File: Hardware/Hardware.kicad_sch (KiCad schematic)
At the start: 46 parts, among them J1 ILI9341, J2 RJ45_LED_Shielded, J3 USB_A, J5 Conn_01x06_Pin, SW1 SW_SPST, SW14 SW_Push, SW2 SW_Push, SW3 SW_Push, SW4 SW_Push, SW5 SW_Push, SW6 SW_Push, SW7 SW_Push, U1 TMR-0511, U2 ATA6561, U3 Teensy4.1_DEV-16771, U4 ESP32-WROOM-32UE, U5 ASSR-1218, U6 ASSR-1218

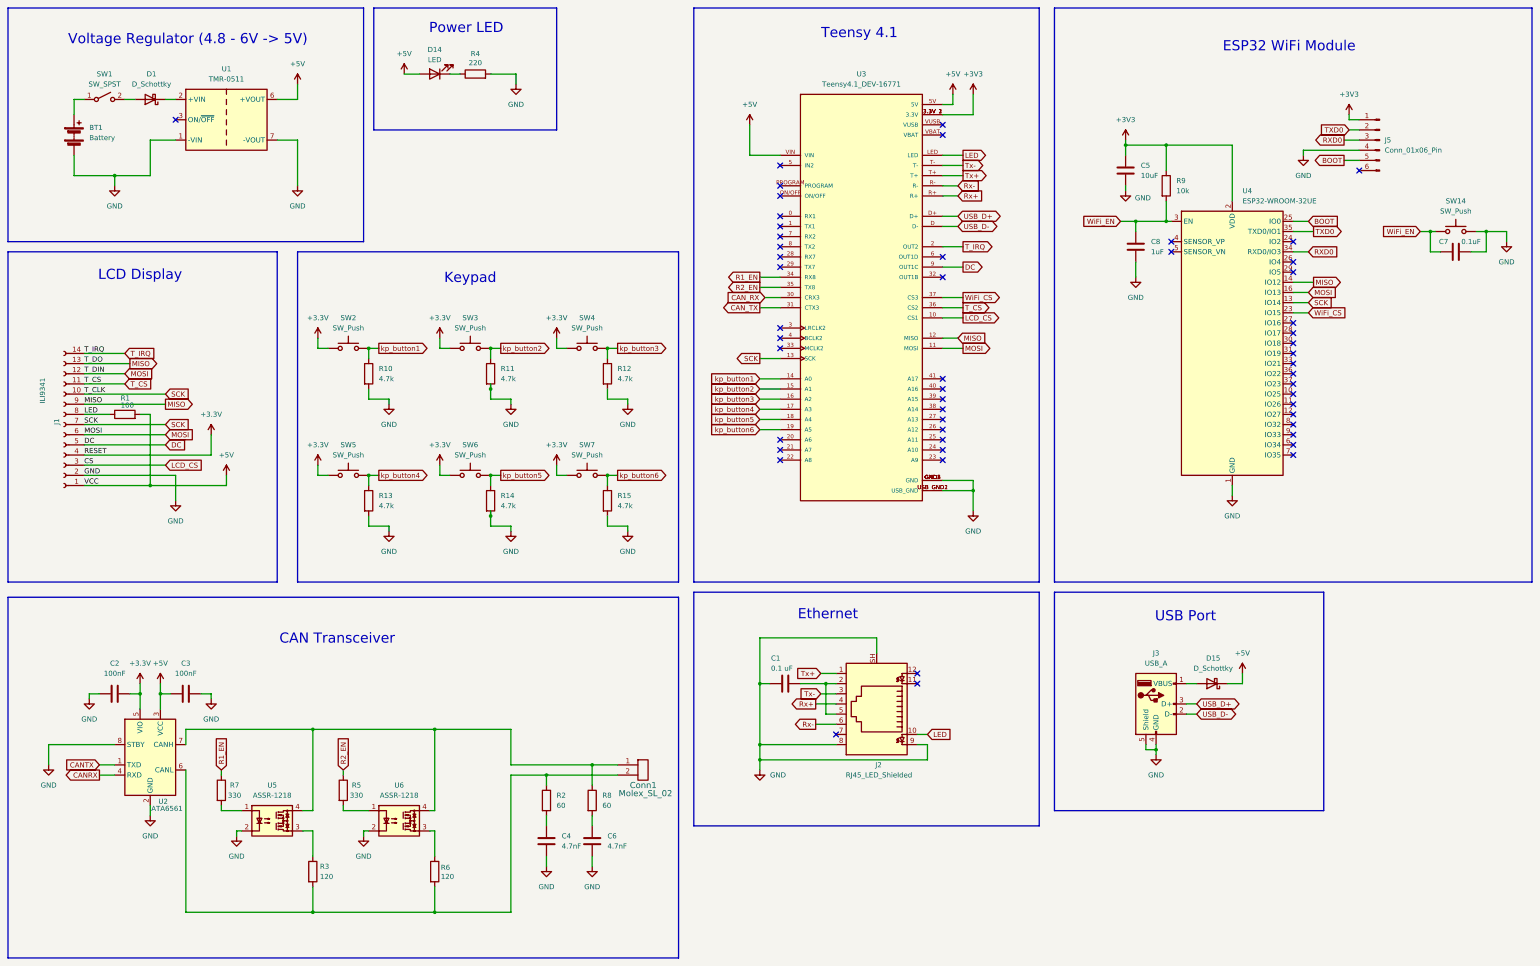
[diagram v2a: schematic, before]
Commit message: added mounting holes and fixed stuff
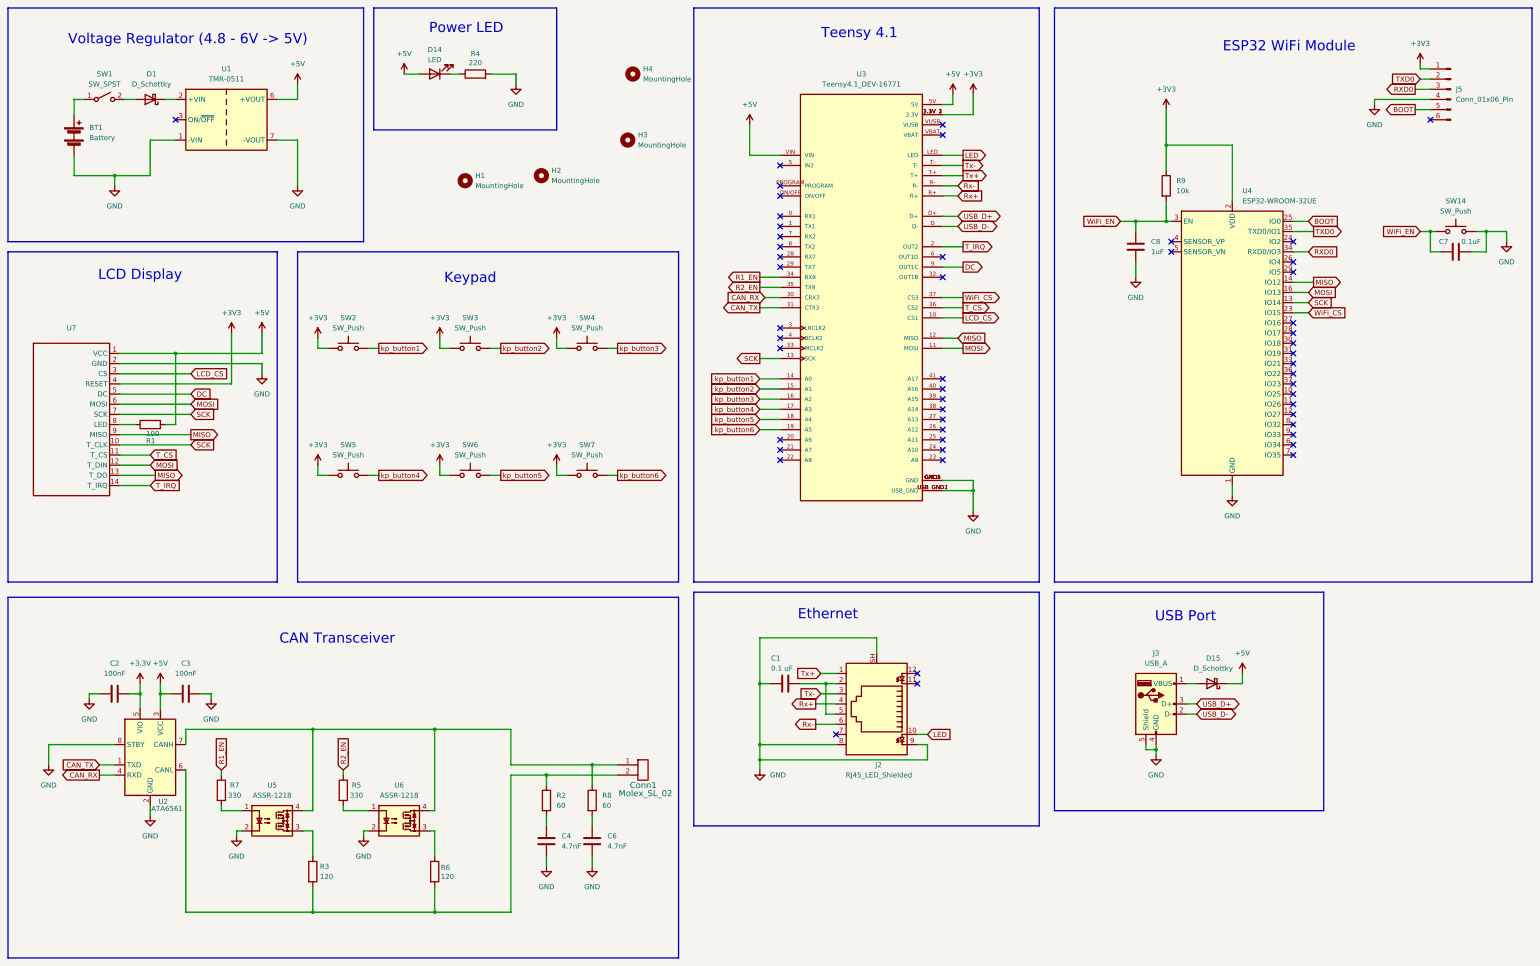
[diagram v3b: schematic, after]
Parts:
- removed C5: 10uF, Capacitor_SMD:C_0603_1608Metric_Pad1.08x0.95mm_HandSolder, symbol Device:C
- removed J1: ILI9341, Connector_PinSocket_2.54mm:PinSocket_1x14_P2.54mm_Vertical, symbol Connector:Conn_01x14_Socket
- removed R10, R11, R12, R13, R14, R15: 4.7k, Resistor_SMD:R_0603_1608Metric_Pad0.98x0.95mm_HandSolder, symbol Device:R
- added H1, H2, H3, H4: MountingHole, MRDT_Drill_Holes:4_40_Hole, symbol Mechanical:MountingHole
- added U7: ~, sw_spst:DISPLAY_ILI9341_TOUCH_32, symbol sw_spst:DISPLAY_ILI9341_TOUCH_32
- BT1: footprint Connector_Wire:SolderWire-0.15sqmm_1x02_P4mm_D0.5mm_OD1.5mm_Relief -> MRDT_Connectors:MOLEX_SL_02_Horizontal
- Conn1: footprint MRDT_Connectors:MOLEX_SL_02_Vertical -> MRDT_Connectors:MOLEX_SL_02_Horizontal
- SW1: footprint sw_spst:SOIC450P1000X730-4N -> Button_Switch_THT:SW_Slide_SPDT_Angled_CK_OS102011MA1Q
- U3: footprint MRDT_Shields:Teensy_4_1_Ethernet -> MRDT_Shields:Teensy_4_1
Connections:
- net CANRX is gone; now on net CAN_RX: U2.4 (RXD)
- net CANTX is gone; now on net CAN_TX: U2.1 (TXD)
- net +3.3V: no longer SW2.1, SW3.1, SW4.1, SW5.1, SW6.1, SW7.1
- net +3V3: now also SW2.1, SW3.1, SW4.1, SW5.1, SW6.1, SW7.1, U7.4 (RESET)
- net +5V: now also U7.1 (VCC)
- net DC: now also U7.5 (DC)
- net GND: now also U7.2 (GND)
- net LCD_CS: now also U7.3 (CS)
- net LED: no longer R1.1
- net MISO: now also U7.13 (T_DO), U7.9 (MISO)
- net MOSI: now also U7.12 (T_DIN), U7.6 (MOSI)
- net SCK: now also U7.10 (T_CLK), U7.7 (SCK)
- net T_CS: now also U7.11 (T_CS)
- net T_IRQ: now also U7.14 (T_IRQ)
- new net: R1.1, U7.8 (LED)
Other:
- moved on the sheet: J5, R1

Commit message: finished up the layout and cleaned up libraries
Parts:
- removed C7: 0.1uF, Capacitor_SMD:C_0603_1608Metric_Pad1.08x0.95mm_HandSolder, symbol Device:C
- removed D1, D15: D_Schottky, MRDT_Passives:SOT-23_Diode, symbol Device:D_Schottky
- added D1, D2: D_Schottky_ZLLS500, Tester:D_Schottky_ZLLS500, symbol Tester:D_Schottky_ZLLS500
- added H5, H6: MountingHole, MRDT_Drill_Holes:4_40_Hole, symbol Mechanical:MountingHole
- SW2, SW3, SW4, SW5, SW6, SW7: footprint Button_Switch_SMD:SW_SPST_TL3305A -> Tester:SW_SPST_TL3301
- U7: footprint sw_spst:DISPLAY_ILI9341_TOUCH_32 -> Tester:DISPLAY_ILI9341_TOUCH_32
- renumbered C6 to C5, C8 to C6, D14 to D3, SW14 to SW8
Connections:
- net +3V3: no longer SW2.1, SW3.1, SW4.1, SW5.1, SW6.1, SW7.1
- net +5V: now also D2.1 (K)
- net GND: now also SW2.1, SW3.1, SW4.1, SW5.1, SW6.1, SW7.1
- net WiFi_EN: now also U3.33 (MCLK2)
- net at SW1.2 (B): now also D1.3 (A)
- net at J3.1 (VBUS): now also D2.3 (A)
- net at U1.2 (+VIN): now also D1.1 (K)
- net kp_button1 renamed KP_ACCEPT
- net kp_button2 renamed KP_BACK
- net kp_button3 renamed KP_RIGHT
- net kp_button4 renamed KP_DOWN
- net KP_DOWN: now also SW6.2; no longer SW5.2
- net kp_button5 renamed KP_UP
- net KP_UP: now also SW5.2; no longer SW6.2
- net kp_button6 renamed KP_LEFT
- no-connect marks 52 -> 51

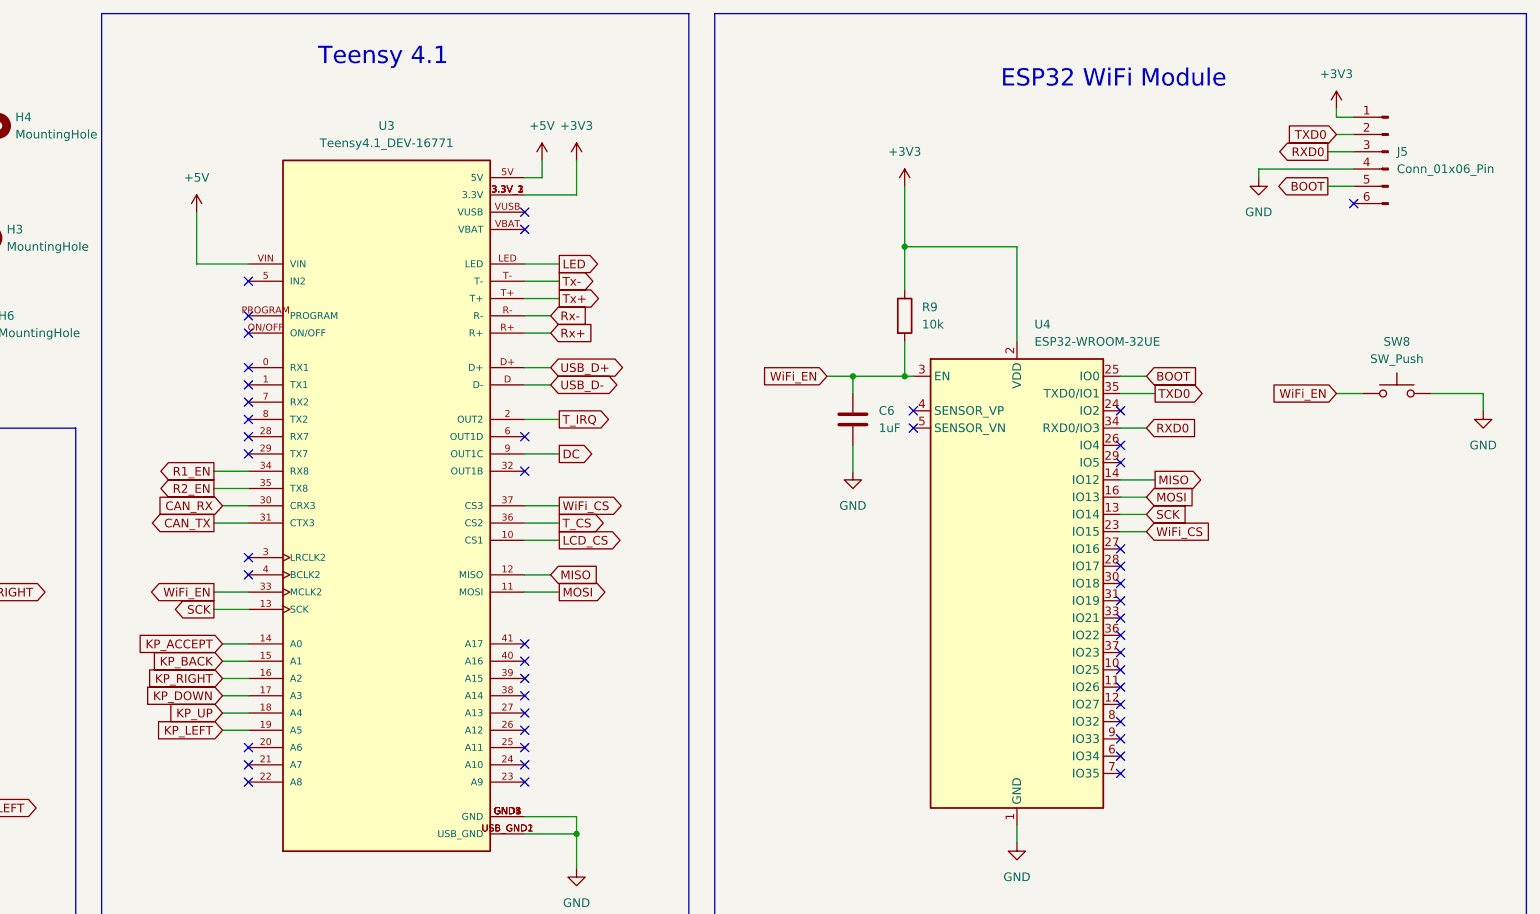
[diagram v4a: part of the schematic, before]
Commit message: swapped buck and esp32 to make traces shorter
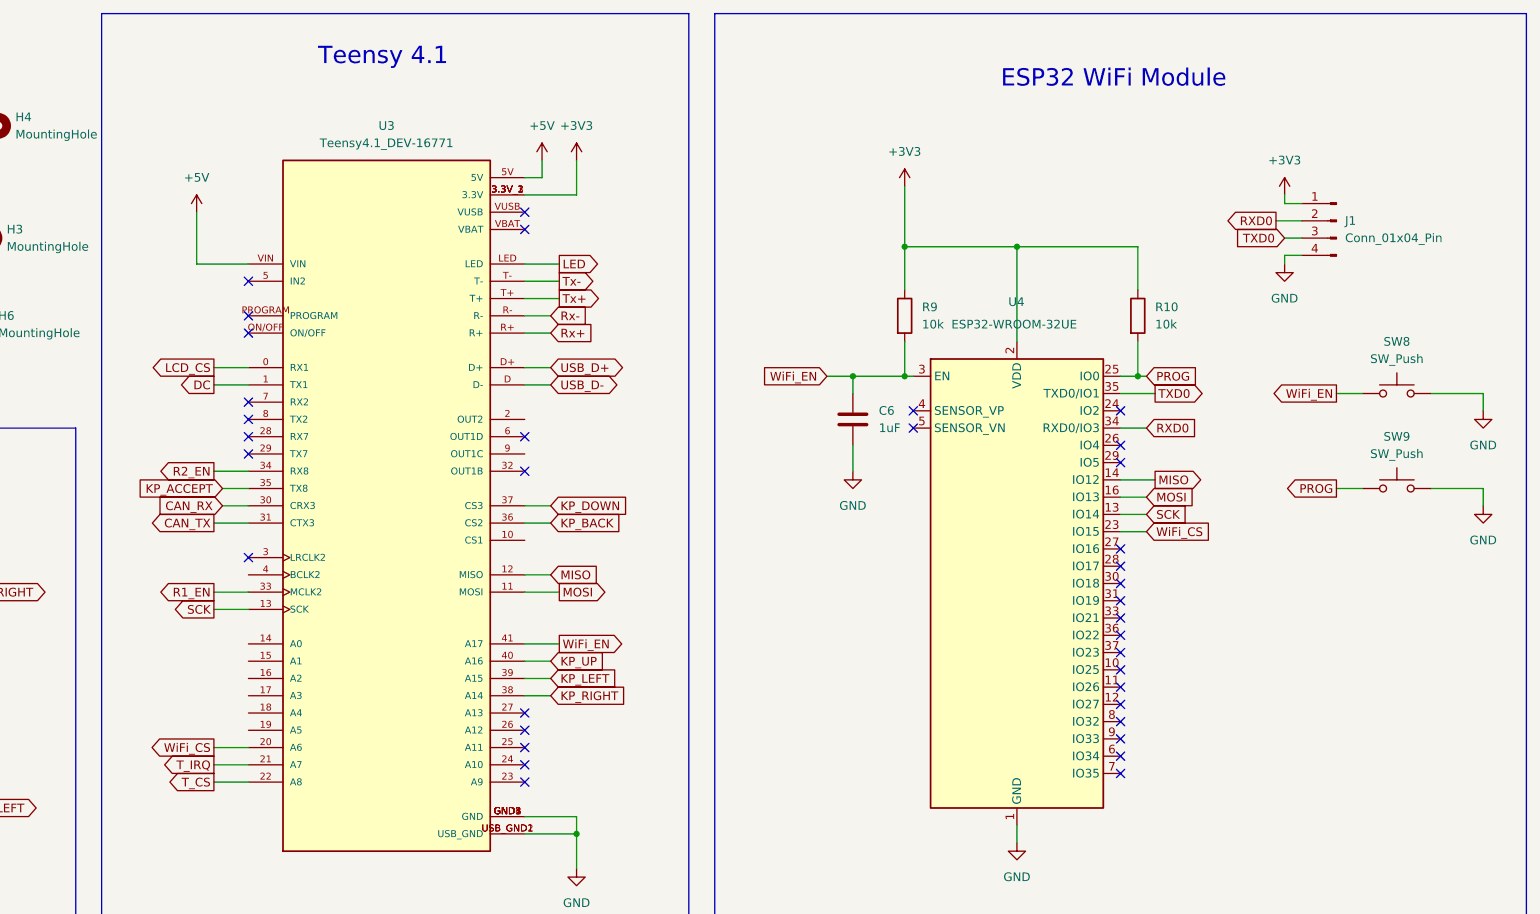
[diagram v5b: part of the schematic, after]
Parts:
- removed J5: Conn_01x06_Pin, Connector_PinHeader_2.54mm:PinHeader_1x06_P2.54mm_Vertical, symbol Connector:Conn_01x06_Pin
- added J1: Conn_01x04_Pin, Connector_PinHeader_2.54mm:PinHeader_1x04_P2.54mm_Vertical, symbol Connector:Conn_01x04_Pin
- added R10: 10k, Resistor_SMD:R_0603_1608Metric_Pad0.98x0.95mm_HandSolder, symbol Device:R
- added SW9: SW_Push, Button_Switch_SMD:SW_SPST_TL3305A, symbol Switch:SW_Push
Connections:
- net +3V3: now also J1.1 (Pin_1), R10.1
- net DC: now also U3.1 (TX1); no longer U3.9 (OUT1C)
- net GND: now also J1.4 (Pin_4), SW9.2
- net KP_ACCEPT: now also U3.35 (TX8); no longer U3.14 (A0)
- net KP_BACK: now also U3.36 (CS2); no longer U3.15 (A1)
- net KP_DOWN: now also U3.37 (CS3); no longer U3.17 (A3)
- net KP_LEFT: now also U3.39 (A15); no longer U3.19 (A5)
- net KP_RIGHT: now also U3.38 (A14); no longer U3.16 (A2)
- net KP_UP: now also U3.40 (A16); no longer U3.18 (A4)
- net LCD_CS: now also U3.0 (RX1); no longer U3.10 (CS1)
- net R1_EN: now also U3.33 (MCLK2); no longer U3.34 (RX8)
- net R2_EN: now also U3.34 (RX8); no longer U3.35 (TX8)
- net RXD0: now also J1.2 (Pin_2)
- net TXD0: now also J1.3 (Pin_3)
- net T_CS: now also U3.22 (A8); no longer U3.36 (CS2)
- net T_IRQ: now also U3.21 (A7); no longer U3.2 (OUT2)
- net WiFi_CS: now also U3.20 (A6); no longer U3.37 (CS3)
- net WiFi_EN: now also U3.41 (A17); no longer U3.33 (MCLK2)
- net BOOT renamed PROG
- net PROG: now also R10.2, SW9.1
- no-connect marks 51 -> 40

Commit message: changed battery case to through-hole pcb mount
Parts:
- BT1: footprint MRDT_Connectors:MOLEX_SL_02_Horizontal -> Tester:Bat_4xAA_MP000327
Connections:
- no-connect marks 40 -> 50
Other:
- moved on the sheet: H1, H2, H3, H4, H5, H6
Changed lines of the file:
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@@
 	)
 	(no_connect
+		(at 215.9 97.79)
+	)
+	(no_connect
+		(at 215.9 118.11)
+	)
+	(no_connect
+		(at 215.9 110.49)
+	)
+	(no_connect
 		(at 256.54 77.47)
 	)
@@
 	)
 	(no_connect
+		(at 256.54 92.71)
+	)
+	(no_connect
 		(at 215.9 80.01)
 	)
@@
 	)
 	(no_connect
+		(at 215.9 115.57)
+	)
+	(no_connect
 		(at 215.9 74.93)
 	)
@@
 	)
 	(no_connect
+		(at 215.9 107.95)
+	)
+	(no_connect
 		(at 215.9 72.39)
 	)
@@
 	)
 	(no_connect
+		(at 256.54 80.01)
+	)
+	(no_connect
 		(at 256.54 123.19)
 	)
@@
 	)
 	(no_connect
+		(at 256.54 74.93)
+	)
+	(no_connect
+		(at 215.9 113.03)
+	)
+	(no_connect
 		(at 313.69 76.2)
 	)
@@
 		(at 344.17 121.92)
 	)
+	(no_connect
+		(at 215.9 120.65)
+	)
 	(wire
 		(pts
@@
 			)
 		)
-		(property "Footprint" "MRDT_Connectors:MOLEX_SL_02_Horizontal"
+		(property "Footprint" "Tester:Bat_4xAA_MP000327"
 			(at 39.37 45.466 90)
 			(effects
@@
 	(symbol
 		(lib_id "Mechanical:MountingHole")
-		(at 156.21 57.15 0)
+		(at 142.24 53.34 0)
 		(unit 1)
 		(exclude_from_sim yes)
@@
 		(fields_autoplaced yes)
 		(property "Reference" "H2"
-			(at 158.75 55.8799 0)
+			(at 144.78 52.0699 0)
 			(effects
 				(font
@@
 		)
 		(property "Value" "MountingHole"
-			(at 158.75 58.4199 0)
+			(at 144.78 54.6099 0)
 			(effects
 				(font
@@
 		)
 		(property "Footprint" "MRDT_Drill_Holes:4_40_Hole"
-			(at 156.21 57.15 0)
+			(at 142.24 53.34 0)
 			(effects
 				(font
@@
 		)
 		(property "Datasheet" "~"
-			(at 156.21 57.15 0)
+			(at 142.24 53.34 0)
 			(effects
 				(font
@@
 		)
 		(property "Description" "Mounting Hole without connection"
-			(at 156.21 57.15 0)
+			(at 142.24 53.34 0)
 			(effects
 				(font
@@
 	(symbol
 		(lib_id "Mechanical:MountingHole")
-		(at 163.83 68.58 0)
+		(at 142.24 62.23 0)
 		(unit 1)
 		(exclude_from_sim yes)
@@
 		(fields_autoplaced yes)
 		(property "Reference" "H5"
-			(at 166.37 67.3099 0)
+			(at 144.78 60.9599 0)
 			(effects
 				(font
@@
 		)
 		(property "Value" "MountingHole"
-			(at 166.37 69.8499 0)
+			(at 144.78 63.4999 0)
 			(effects
 				(font
@@
 		)
 		(property "Footprint" "MRDT_Drill_Holes:4_40_Hole"
-			(at 163.83 68.58 0)
+			(at 142.24 62.23 0)
 			(effects
 				(font
@@
 		)
 		(property "Datasheet" "~"
-			(at 163.83 68.58 0)
+			(at 142.24 62.23 0)
 			(effects
 				(font
@@
 		)
 		(property "Description" "Mounting Hole without connection"
-			(at 163.83 68.58 0)
+			(at 142.24 62.23 0)
 			(effects
 				(font
@@
 	(symbol
 		(lib_id "Mechanical:MountingHole")
-		(at 177.8 48.26 0)
+		(at 161.29 53.34 0)
 		(unit 1)
 		(exclude_from_sim yes)
@@
 		(fields_autoplaced yes)
 		(property "Reference" "H3"
-			(at 180.34 46.9899 0)
+			(at 163.83 52.0699 0)
 			(effects
 				(font
@@
 		)
 		(property "Value" "MountingHole"
-			(at 180.34 49.5299 0)
+			(at 163.83 54.6099 0)
 			(effects
 				(font
@@
 		)
 		(property "Footprint" "MRDT_Drill_Holes:4_40_Hole"
-			(at 177.8 48.26 0)
+			(at 161.29 53.34 0)
 			(effects
 				(font
@@
 		)
 		(property "Datasheet" "~"
-			(at 177.8 48.26 0)
+			(at 161.29 53.34 0)
 			(effects
 				(font
@@
 		)
 		(property "Description" "Mounting Hole without connection"
-			(at 177.8 48.26 0)
+			(at 161.29 53.34 0)
 			(effects
 				(font
@@
 	(symbol
 		(lib_id "Mechanical:MountingHole")
-		(at 179.07 31.75 0)
+		(at 123.19 62.23 0)
 		(unit 1)
 		(exclude_from_sim yes)
@@
 		(fields_autoplaced yes)
 		(property "Reference" "H4"
-			(at 181.61 30.4799 0)
+			(at 125.73 60.9599 0)
 			(effects
 				(font
@@
 		)
 		(property "Value" "MountingHole"
-			(at 181.61 33.0199 0)
+			(at 125.73 63.4999 0)
 			(effects
 				(font
@@
 		)
 		(property "Footprint" "MRDT_Drill_Holes:4_40_Hole"
-			(at 179.07 31.75 0)
+			(at 123.19 62.23 0)
 			(effects
 				(font
@@
 		)
 		(property "Datasheet" "~"
-			(at 179.07 31.75 0)
+			(at 123.19 62.23 0)
 			(effects
 				(font
@@
 		)
 		(property "Description" "Mounting Hole without connection"
-			(at 179.07 31.75 0)
+			(at 123.19 62.23 0)
 			(effects
 				(font
@@
 	(symbol
 		(lib_id "Mechanical:MountingHole")
-		(at 176.53 60.96 0)
+		(at 161.29 62.23 0)
 		(unit 1)
 		(exclude_from_sim yes)
@@
 		(fields_autoplaced yes)
 		(property "Reference" "H6"
-			(at 179.07 59.6899 0)
+			(at 163.83 60.9599 0)
 			(effects
 				(font
@@
 		)
 		(property "Value" "MountingHole"
-			(at 179.07 62.2299 0)
+			(at 163.83 63.4999 0)
 			(effects
 				(font
@@
 		)
 		(property "Footprint" "MRDT_Drill_Holes:4_40_Hole"
-			(at 176.53 60.96 0)
+			(at 161.29 62.23 0)
 			(effects
 				(font
@@
 		)
 		(property "Datasheet" "~"
-			(at 176.53 60.96 0)
+			(at 161.29 62.23 0)
 			(effects
 				(font
@@
 		)
 		(property "Description" "Mounting Hole without connection"
-			(at 176.53 60.96 0)
+			(at 161.29 62.23 0)
 			(effects
 				(font
@@
 	(symbol
 		(lib_id "Mechanical:MountingHole")
-		(at 137.16 58.42 0)
+		(at 123.19 53.34 0)
 		(unit 1)
 		(exclude_from_sim yes)
@@
 		(fields_autoplaced yes)
 		(property "Reference" "H1"
-			(at 139.7 57.1499 0)
+			(at 125.73 52.0699 0)
 			(effects
 				(font
@@
 		)
 		(property "Value" "MountingHole"
-			(at 139.7 59.6899 0)
+			(at 125.73 54.6099 0)
 			(effects
 				(font
@@
 		)
 		(property "Footprint" "MRDT_Drill_Holes:4_40_Hole"
-			(at 137.16 58.42 0)
+			(at 123.19 53.34 0)
 			(effects
 				(font
@@
 		)
 		(property "Datasheet" "~"
-			(at 137.16 58.42 0)
+			(at 123.19 53.34 0)
 			(effects
 				(font
@@
 		)
 		(property "Description" "Mounting Hole without connection"
-			(at 137.16 58.42 0)
+			(at 123.19 53.34 0)
 			(effects
 				(font
